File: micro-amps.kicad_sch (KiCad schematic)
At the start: 21 parts, among them J1 Conn_01x04_Pin, J2 Conn_01x01_Socket, J3 Conn_02x04_Odd_Even, J4 Conn_01x01_Socket, J5 Conn_01x01_Socket, J6 Conn_01x01_Socket, SW1 SW_Slide_DPDT, U1 OPA197xDBV

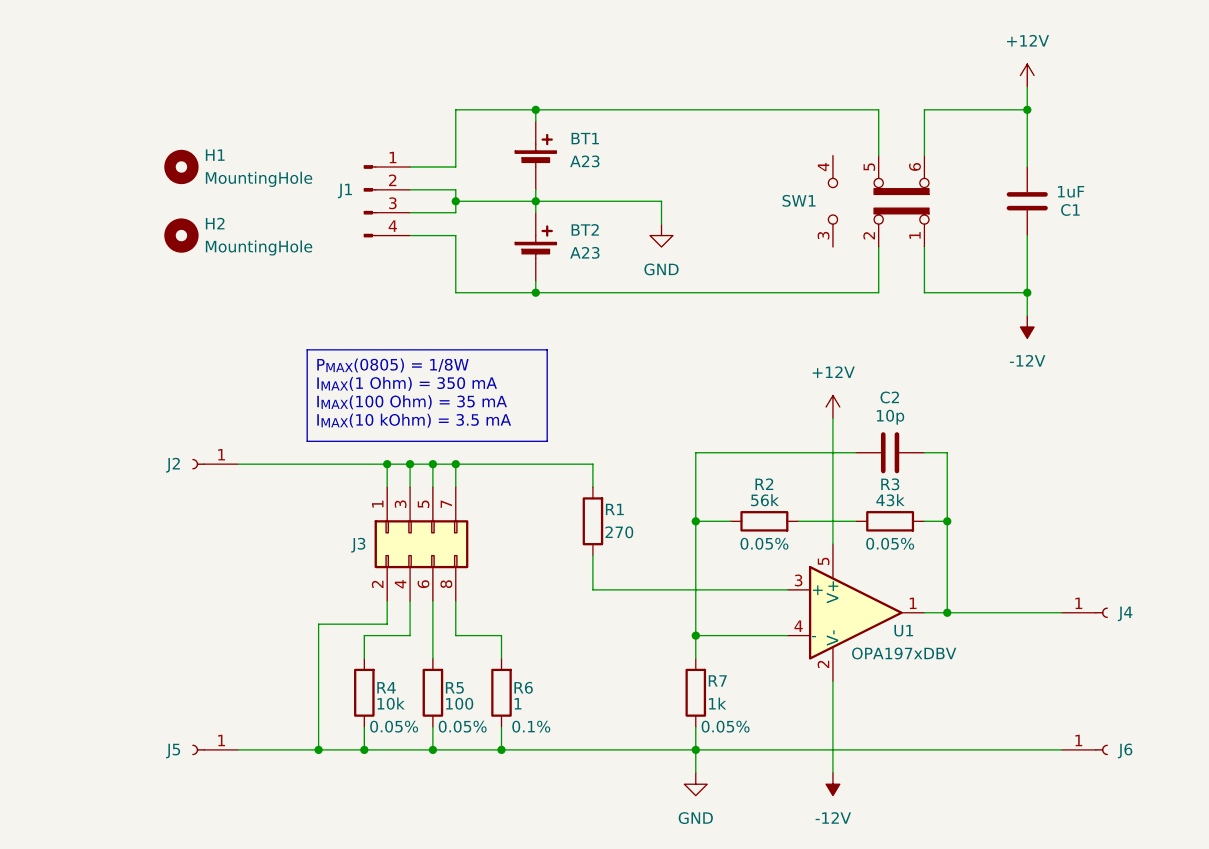
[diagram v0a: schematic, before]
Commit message: Dual OPAMP stage
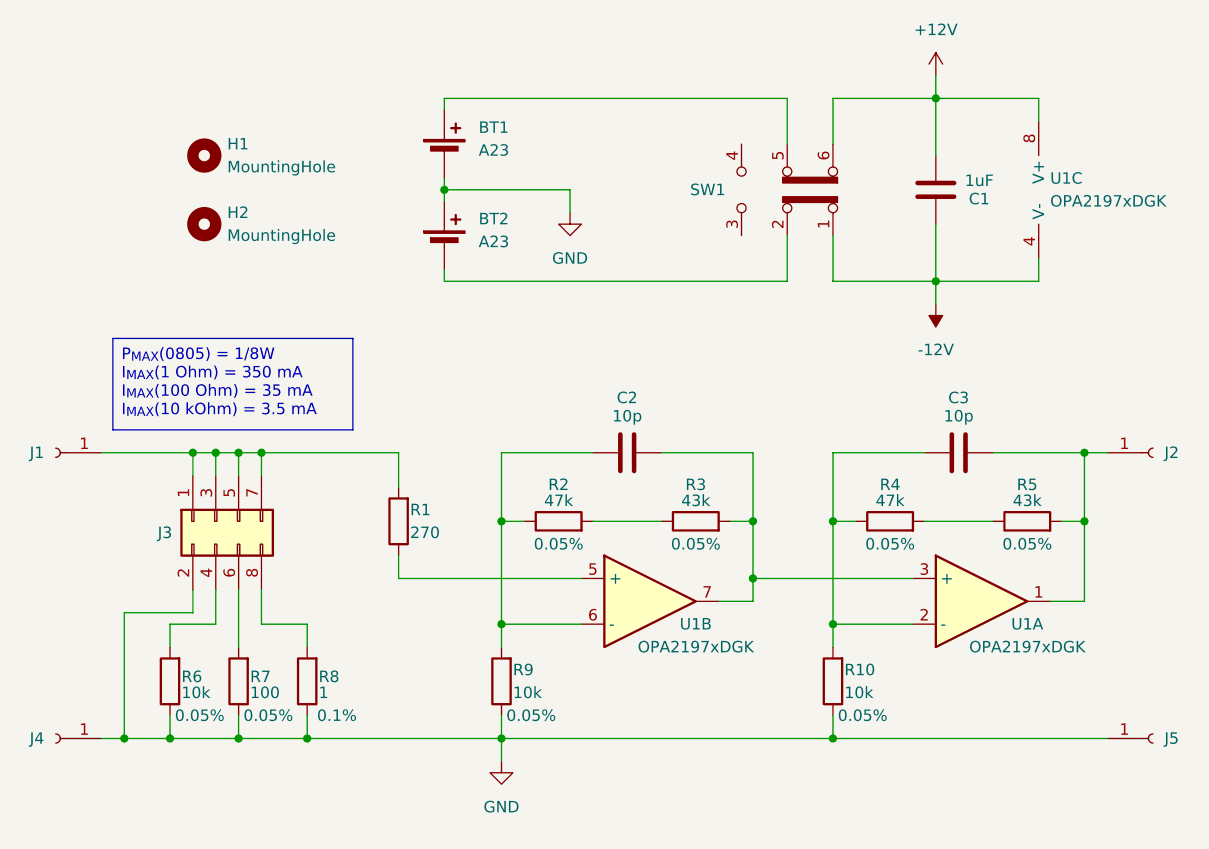
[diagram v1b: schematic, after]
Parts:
- removed J1: Conn_01x04_Pin, Connector_PinHeader_2.54mm:PinHeader_1x04_P2.54mm_Vertical, symbol Connector:Conn_01x04_Pin
- removed U1: OPA197xDBV, Package_TO_SOT_SMD:SOT-23-5_HandSoldering, symbol Amplifier_Operational:OPA197xDBV
- added C3: 10p, Capacitor_SMD:C_0603_1608Metric_Pad1.08x0.95mm_HandSolder, symbol Device:C
- added R10: 10k, Resistor_SMD:R_0603_1608Metric_Pad0.98x0.95mm_HandSolder, symbol Device:R
- added R4: 47k, Resistor_SMD:R_0603_1608Metric_Pad0.98x0.95mm_HandSolder, symbol Device:R
- added R5: 43k, Resistor_SMD:R_0603_1608Metric_Pad0.98x0.95mm_HandSolder, symbol Device:R
- added U1: OPA2197xDGK, Package_SO:VSSOP-8_3x3mm_P0.65mm, symbol Amplifier_Operational:OPA2197xDGK
- R2: value 56k -> 47k
- R9: renamed from R7; value 1k -> 10k
- renumbered J2 to J1, J4 to J2, J5 to J4, J6 to J5, R4 to R6, R5 to R7, R6 to R8
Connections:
- net +12V: now also U1.8 (V+)
- net -12V: now also U1.4 (V-)
- net GND: now also R10.1
- net at C2.1, R3.2: now also U1.3 (+), U1.7; no longer J2.1 (Pin_1)
- net at C2.2, R2.1, R9.2: now also U1.6 (-)
- net at R1.1: now also U1.5 (+)
- new net: C3.2, R10.2, R4.1, U1.2 (-)
- new net: C3.1, J2.1 (Pin_1), R5.2, U1.1
- new net: R4.2, R5.1
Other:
- moved on the sheet: BT1, BT2, C1, C2, H1, H2, J1, J2, J3, J4, J5, R1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
